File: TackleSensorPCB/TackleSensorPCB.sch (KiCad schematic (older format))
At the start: 24 parts, among them J1 PJ-037A, J2 Conn_01x03_Male, J3 Conn_01x03_Male, J4 Conn_01x07_Male, Q1 2N7002, Q2 2N7002, SW1 SW_DPST_x2, U1 TPS62172DSG, U2 MSP430FR2433IRGER, U3 MMA8452QR1

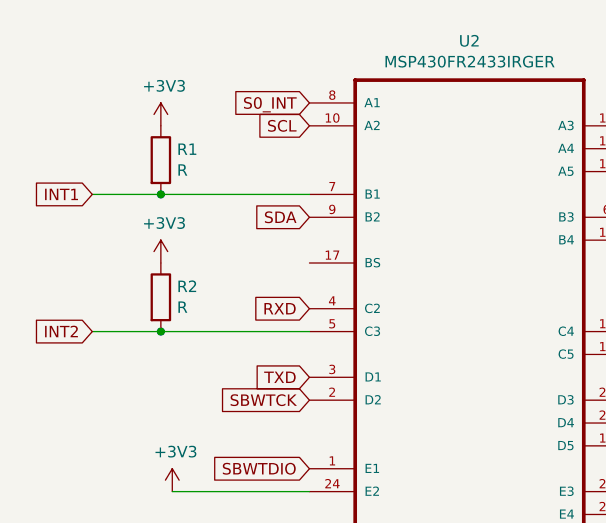
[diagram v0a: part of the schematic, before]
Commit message: Added pull up resistor values
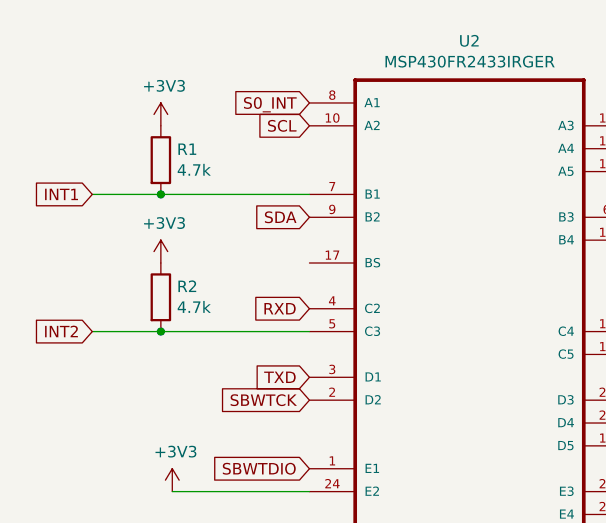
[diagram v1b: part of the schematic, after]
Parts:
- R1, R2: value R -> 4.7k
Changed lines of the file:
@@
 P 1550 2400
 F 0 "R2" H 1620 2446 50  0000 L CNN
-F 1 "R" H 1620 2355 50  0000 L CNN
+F 1 "4.7k" H 1620 2355 50  0000 L CNN
 F 2 "" V 1480 2400 50  0001 C CNN
 F 3 "~" H 1550 2400 50  0001 C CNN
@@
 P 1550 1800
 F 0 "R1" H 1620 1846 50  0000 L CNN
-F 1 "R" H 1620 1755 50  0000 L CNN
+F 1 "4.7k" H 1620 1755 50  0000 L CNN
 F 2 "" V 1480 1800 50  0001 C CNN
 F 3 "~" H 1550 1800 50  0001 C CNN
